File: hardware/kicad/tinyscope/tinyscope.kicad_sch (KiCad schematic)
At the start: 51 parts, among them J1 USB_C_Receptacle_USB2.0, J2 Conn_01x02, J3 Conn_01x02, Q1 PMOS, U1 USBLC6-2SC6_MOD, U2 BQ24075RGT, U3 MAX17048G, U4 TPS54360DDA, U5 TPS63802DLAR

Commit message: feat: hardware: Add tinyscope kicad project. Adds description to TPS63802 3V3 buck-boost converter
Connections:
- net TPS54360_OUT is gone; now on net TPS54360_VOUT: C8.1, C9.1, L1.2, R13.1
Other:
- note added: "Regulation / Rails"
- moved on the sheet: C13, C14, L2, R16, R17, R18, U5

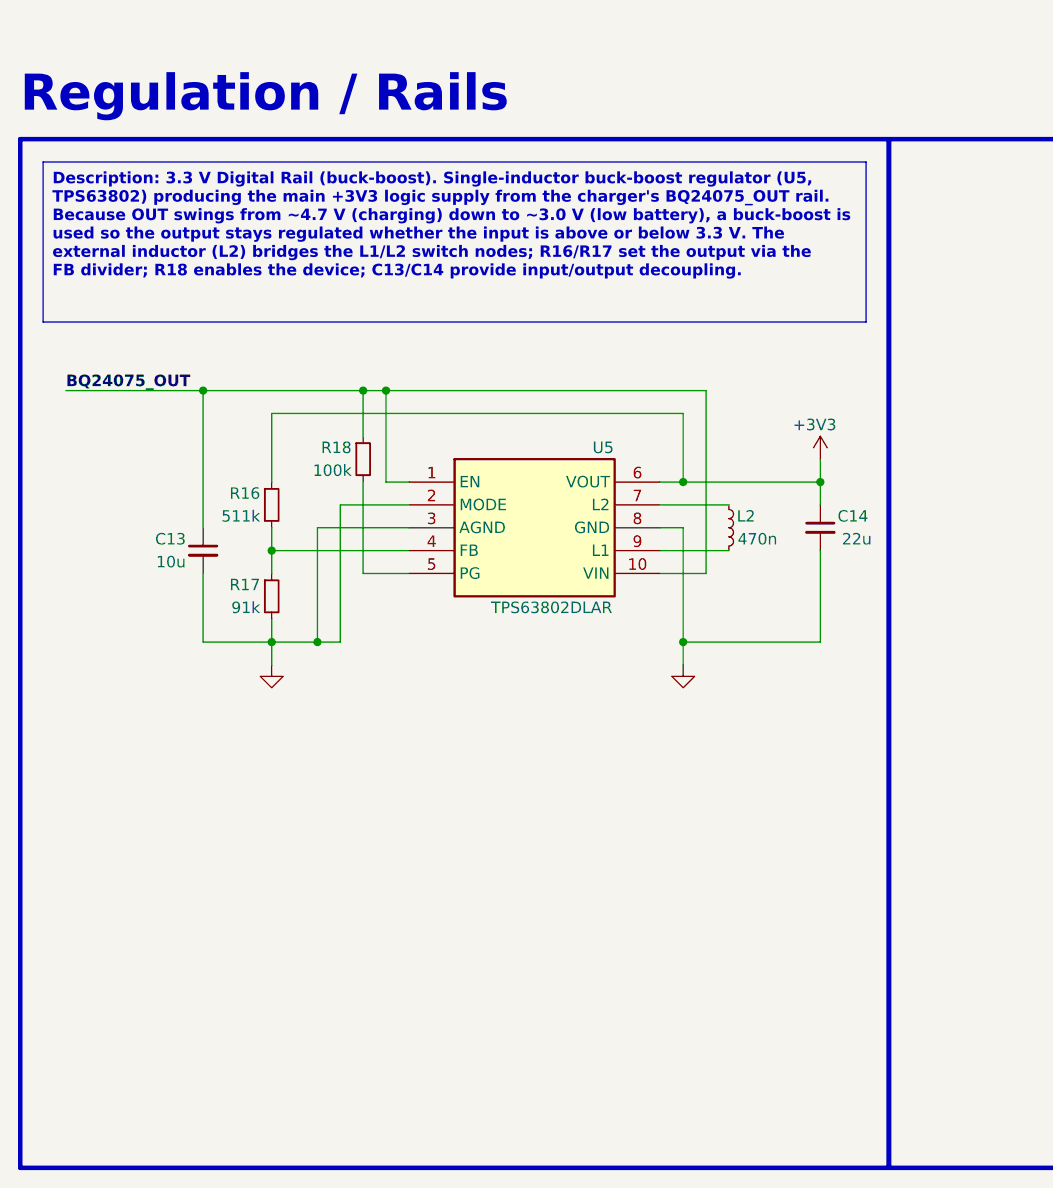
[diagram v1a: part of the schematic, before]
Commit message: feat: hardware: Add tinyscope kicad project. Adds TPS61023 5V boost voltage converter
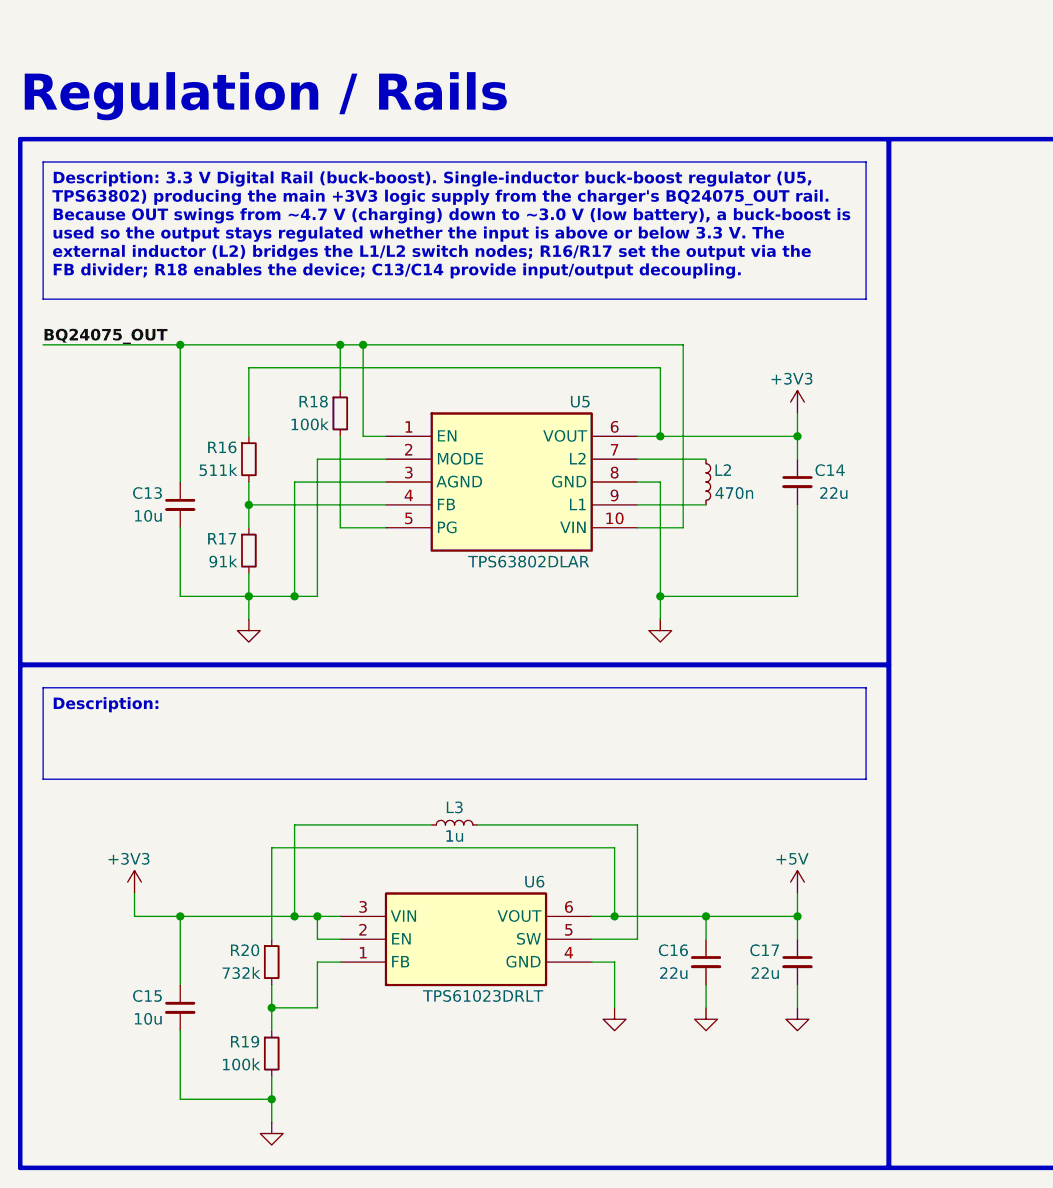
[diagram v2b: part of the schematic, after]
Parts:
- added C15: 10u, symbol Device:C_Small
- added C16, C17: 22u, symbol Device:C_Small
- added L3: 1u, symbol Device:L_Small
- added R19: 100k, symbol Device:R_Small
- added R20: 732k, symbol Device:R_Small
- added U6: TPS61023DRLT, SOTFL50P160X60-6N, symbol TPS61023DRLT:TPS61023DRLT
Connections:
- net +3V3: now also C15.1, L3.1, U6.2 (EN), U6.3 (VIN)
- net GND: now also C15.2, C16.2, C17.2, R19.2, U6.4 (GND)
- new net: R19.1, R20.2, U6.1 (FB)
- new net: L3.2, U6.5 (SW)
- new net +5V: C16.1, C17.1, R20.1, U6.6 (VOUT)
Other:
- moved on the sheet: C13, C14, L2, R16, R17, R18, U5

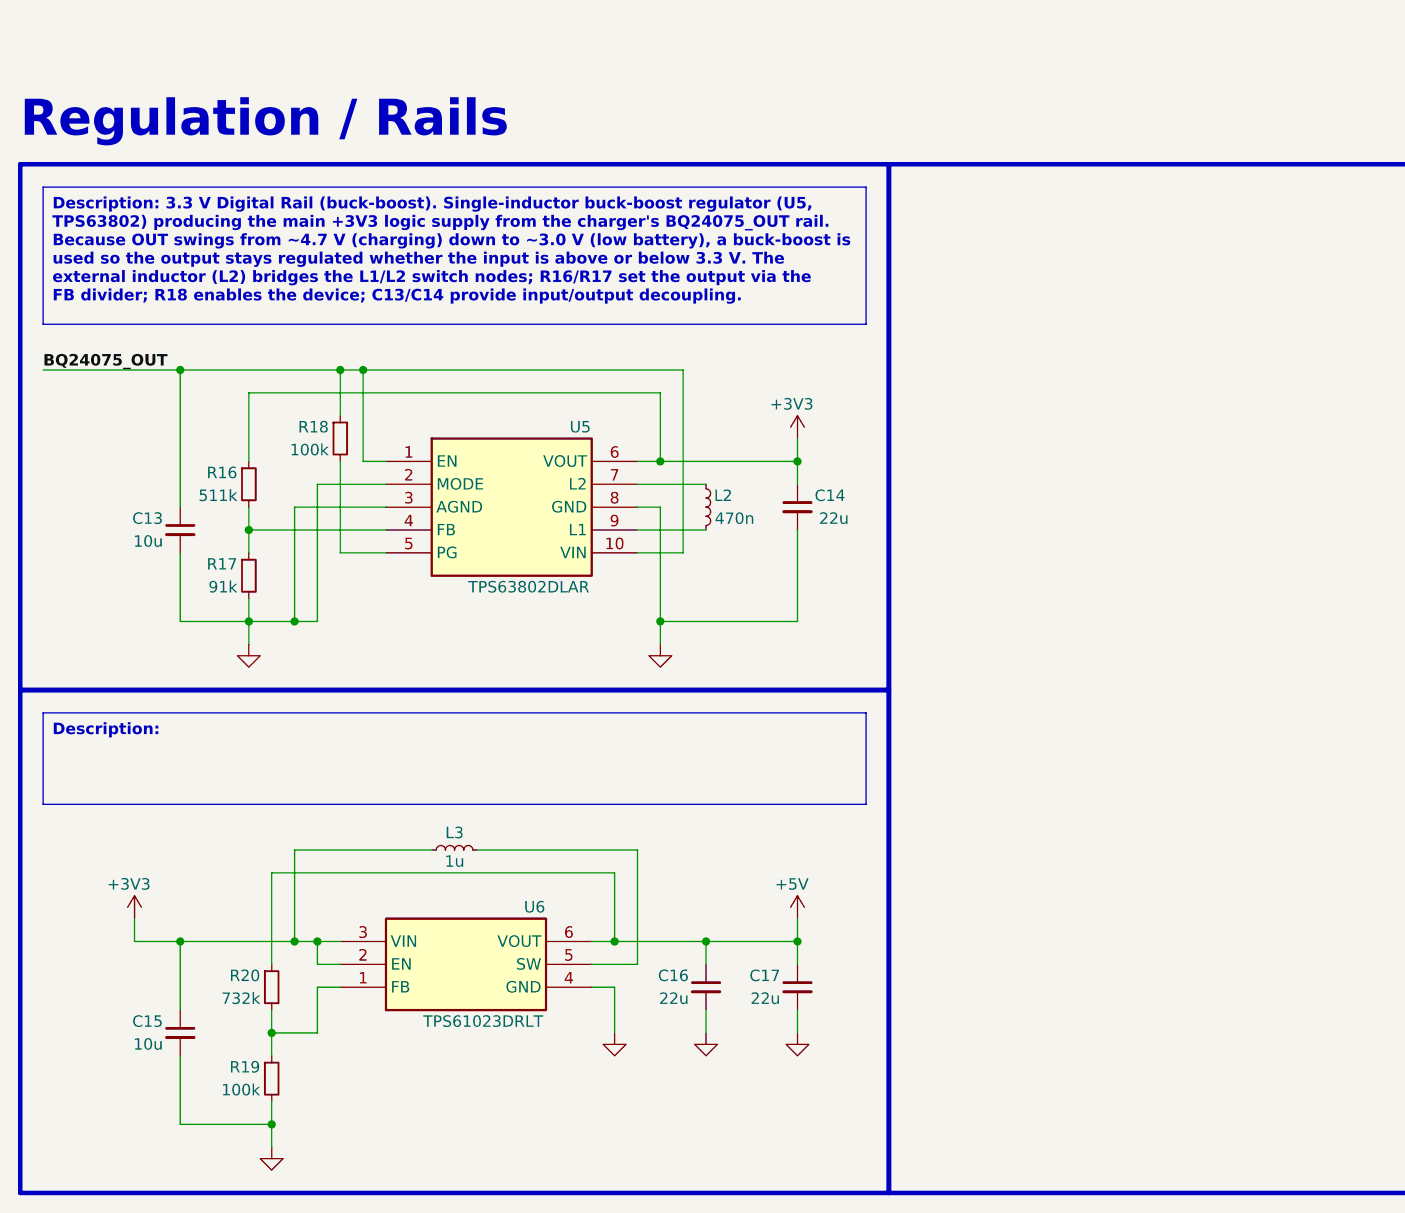
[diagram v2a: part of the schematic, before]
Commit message: feat: hardware: Add tinyscope kicad project. Adds TPS63802 5V buck-boost converter instead of the TPS61023 (which input voltage range is too low)
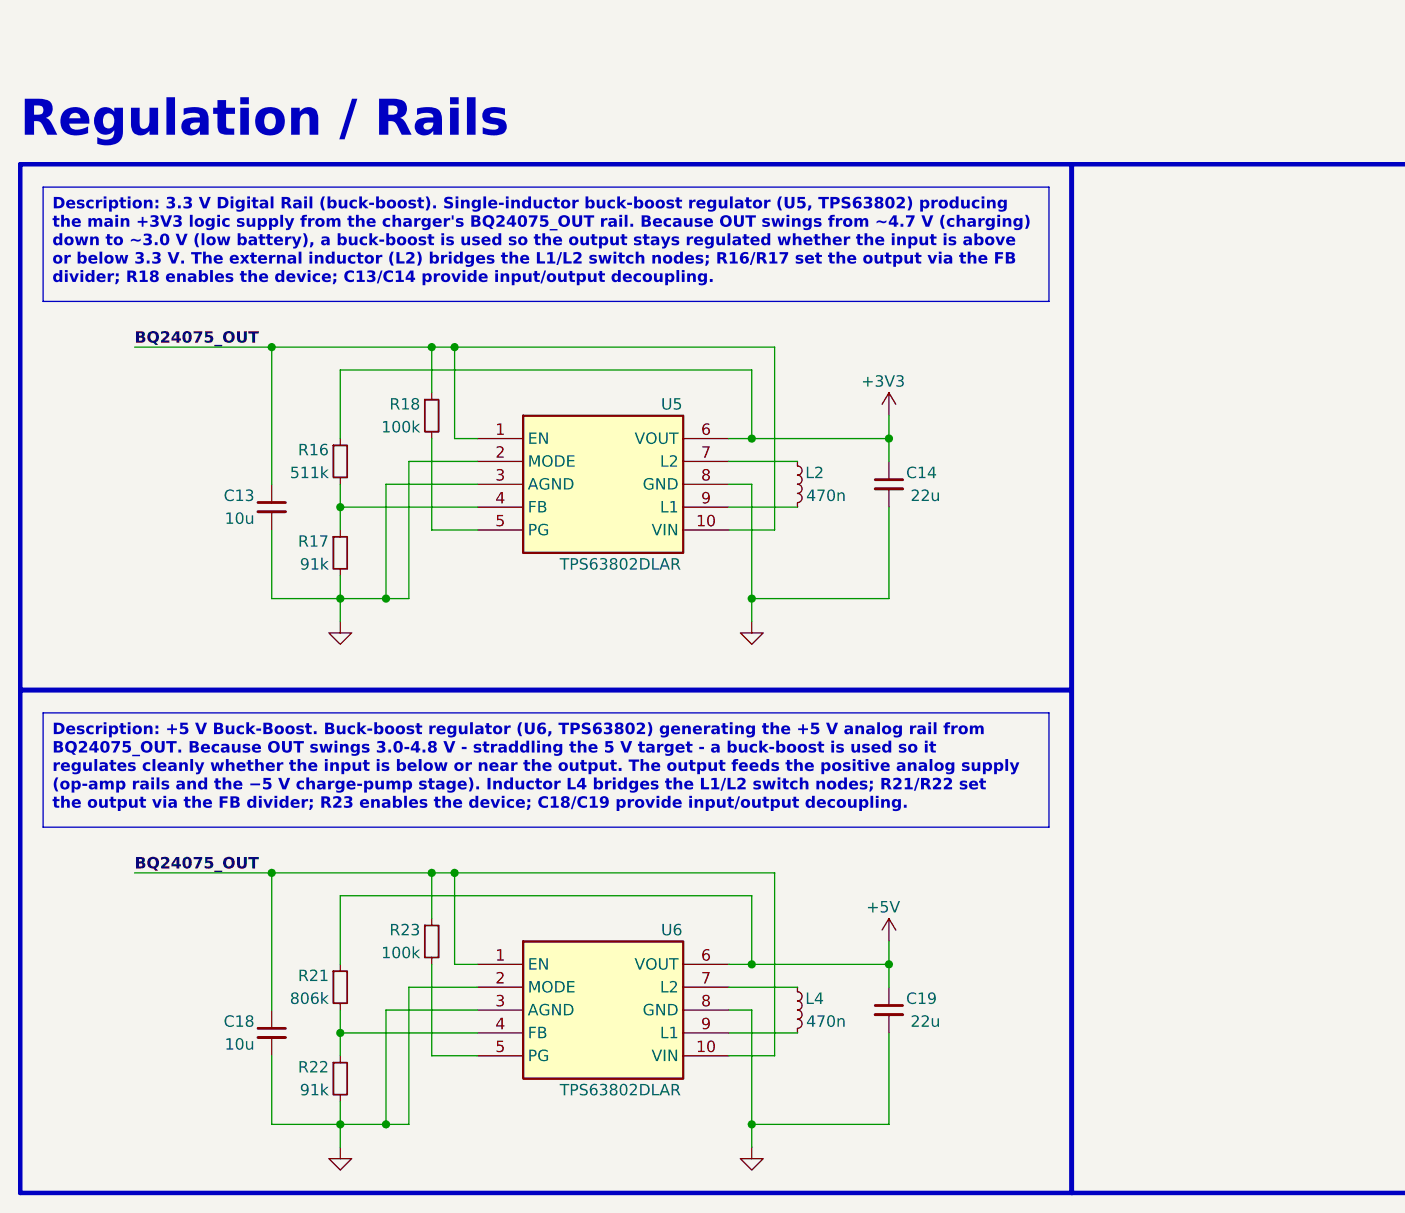
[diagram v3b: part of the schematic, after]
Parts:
- removed C15: 10u, symbol Device:C_Small
- removed C16, C17: 22u, symbol Device:C_Small
- removed L3: 1u, symbol Device:L_Small
- removed R19: 100k, symbol Device:R_Small
- removed R20: 732k, symbol Device:R_Small
- removed U6: TPS61023DRLT, SOTFL50P160X60-6N, symbol TPS61023DRLT:TPS61023DRLT
- added C18: 10u, symbol Device:C_Small
- added C19: 22u, symbol Device:C_Small
- added L4: 470n, symbol Device:L_Small
- added R21: 806k, symbol Device:R_Small
- added R22: 91k, symbol Device:R_Small
- added R23: 100k, symbol Device:R_Small
- added U6: TPS63802DLAR, TPS63802DLAR, symbol TPS63802DLAR:TPS63802DLAR
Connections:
- net +5V: now also C19.1, R21.1, U6.6 (VOUT)
- net BQ24075_OUT: now also C18.1, R23.1, U6.1 (EN), U6.10 (VIN)
- net GND: now also C18.2, C19.2, R22.2, U6.2 (MODE), U6.3 (AGND), U6.8 (GND)
- new net: R21.2, R22.1, U6.4 (FB)
- new net: R23.2, U6.5 (PG)
- new net: L4.1, U6.7 (L2)
- new net: L4.2, U6.9 (L1)
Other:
- moved on the sheet: C13, C14, L2, R16, R17, R18, U5

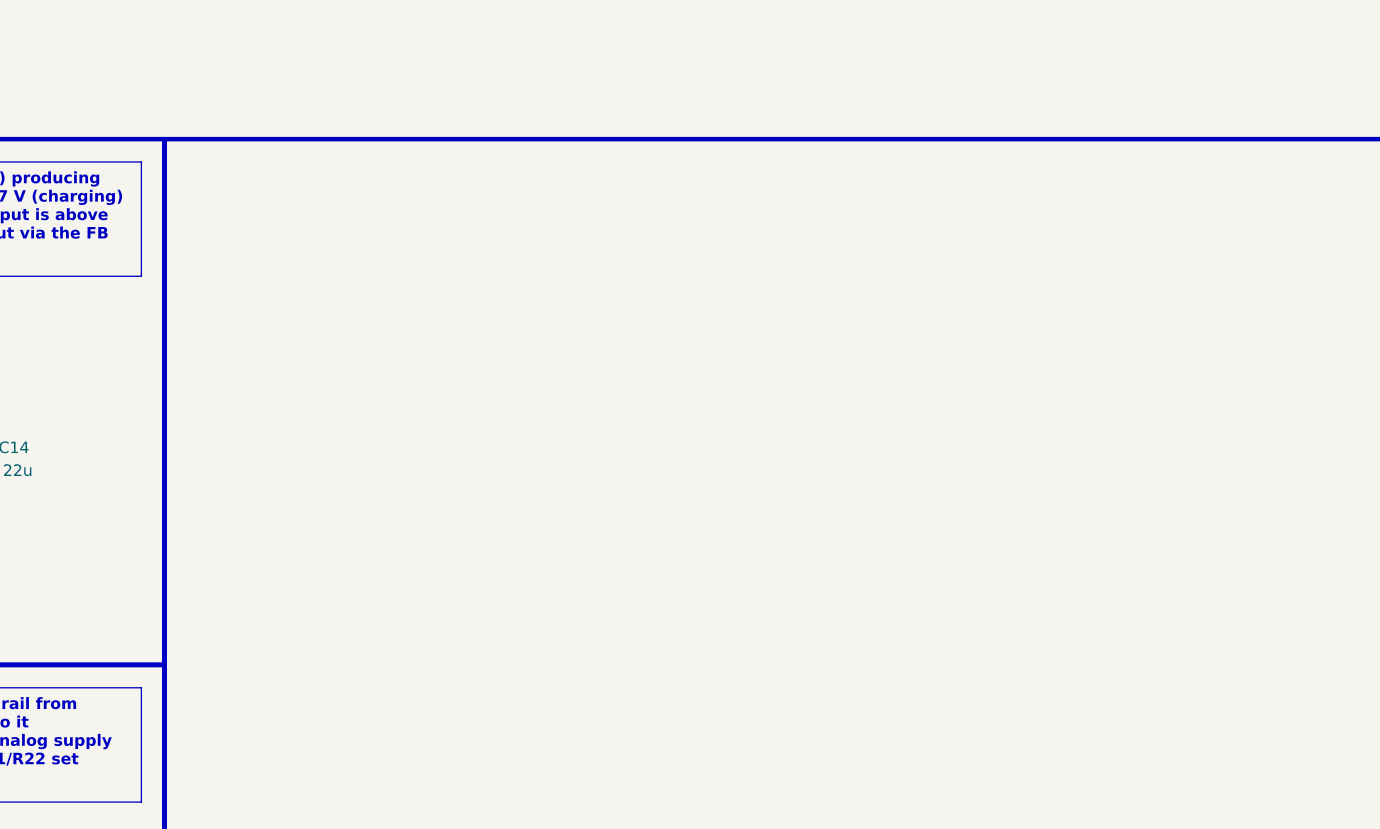
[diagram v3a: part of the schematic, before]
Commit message: feat: hardware: Add tinyscope kicad project. Adds LM27761 -5V Switched-Capacitor Voltage Inverter
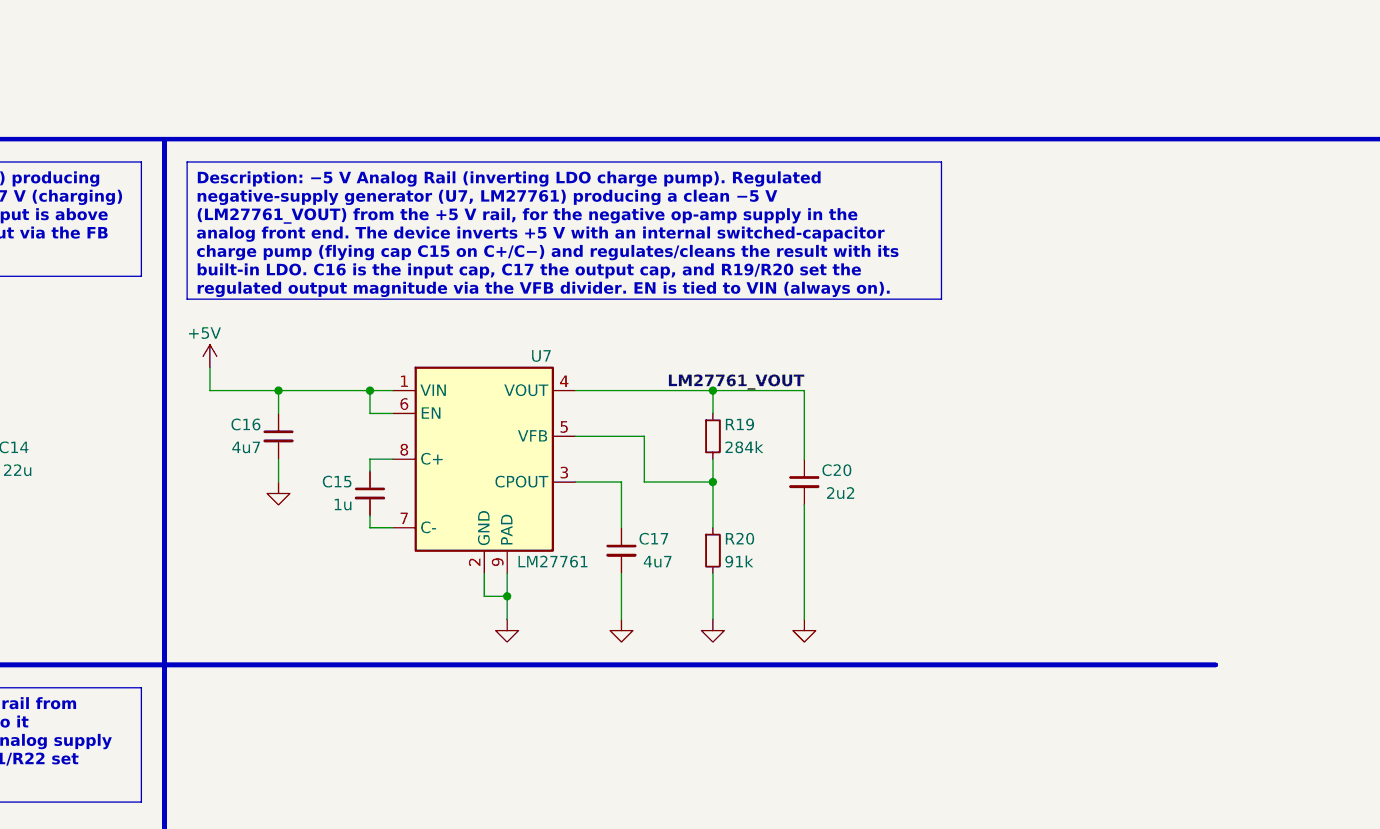
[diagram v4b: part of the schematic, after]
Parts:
- added C15: 1u, symbol Device:C_Small
- added C16, C17: 4u7, symbol Device:C_Small
- added C20: 2u2, symbol Device:C_Small
- added R19: 284k, symbol Device:R_Small
- added R20: 91k, symbol Device:R_Small
- added U7: LM27761, Package_SON:WSON-8-1EP_2x2mm_P0.5mm_EP0.9x1.6mm, symbol Regulator_SwitchedCapacitor:LM27761
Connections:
- net +5V: now also C16.1, U7.1 (VIN), U7.6 (EN)
- net GND: now also C16.2, C17.2, C20.2, R20.2, U7.2 (GND), U7.9 (PAD)
- new net: C17.1, U7.3 (CPOUT)
- new net: R19.2, R20.1, U7.5 (VFB)
- new net: C15.2, U7.7 (C-)
- new net: C15.1, U7.8 (C+)
- new net LM27761_VOUT: C20.1, R19.1, U7.4 (VOUT)
